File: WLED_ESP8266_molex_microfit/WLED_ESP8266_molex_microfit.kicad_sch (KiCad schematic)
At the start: 30 parts, among them J1 Molex Micro-fit 2x1, U1 ESP-12F, U2 AP6503, U3 TXS0102DCT, U4 TXS0102DCT

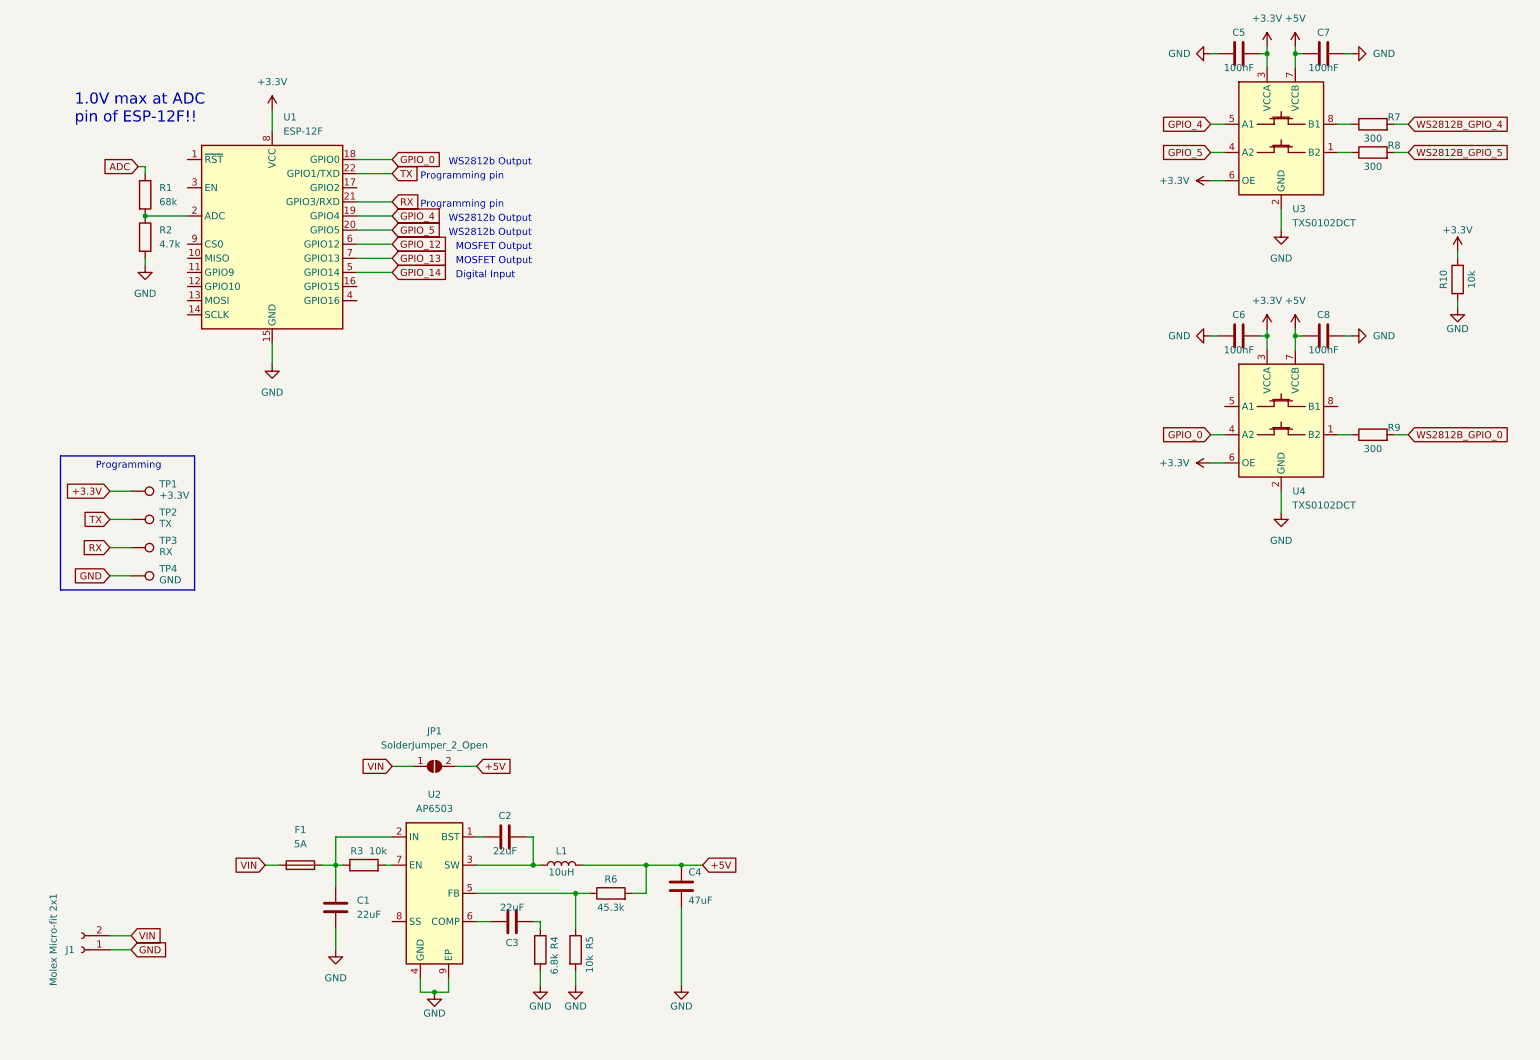
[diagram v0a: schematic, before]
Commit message: schematics updated
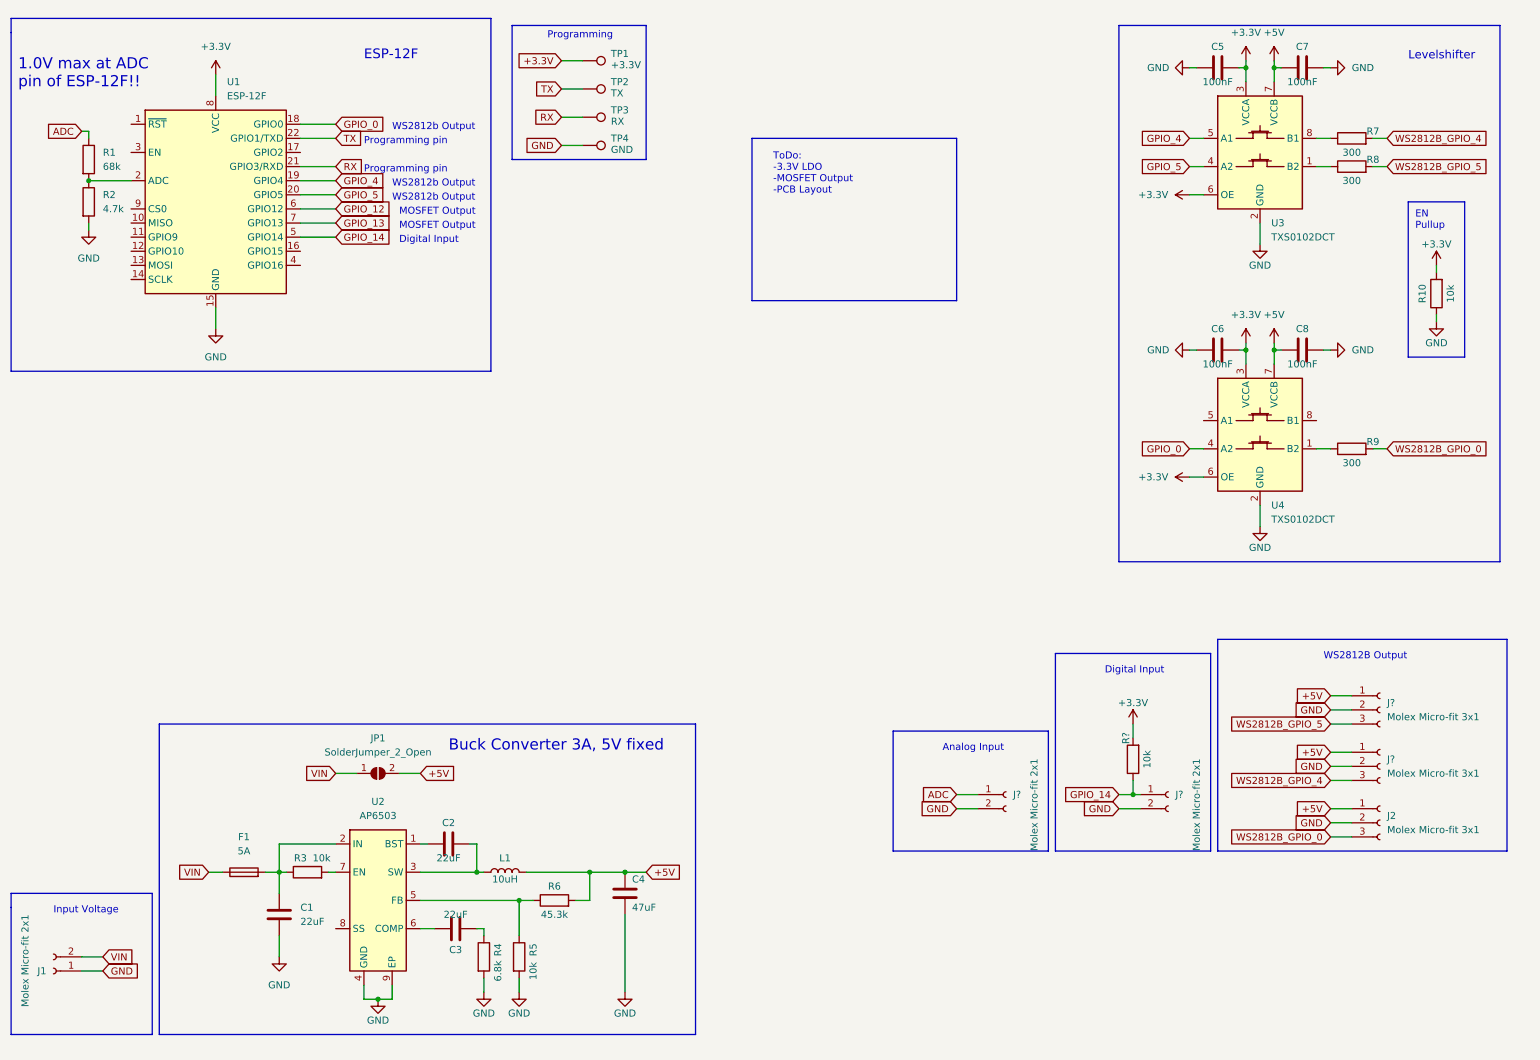
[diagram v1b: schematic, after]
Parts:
- added J2, J? (x2): Molex Micro-fit 3x1, Connector_Molex:Molex_Micro-Fit_3.0_43650-0300_1x03_P3.00mm_Horizontal, symbol Connector:Conn_01x03_Female
- added J? (x2): Molex Micro-fit 2x1, Connector_Molex:Molex_Micro-Fit_3.0_43650-0200_1x02_P3.00mm_Horizontal, symbol Connector:Conn_01x02_Female
- added R?: 10k, Capacitor_SMD:C_0603_1608Metric_Pad1.08x0.95mm_HandSolder, symbol Device:R
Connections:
- net +3V3: now also R?.2
- net +5V: now also J2.1 (Pin_1), J?.1 (Pin_1), J?.1 (Pin_1)
- net ADC: now also J?.1 (Pin_1)
- net GND: now also J2.2 (Pin_2), J?.2 (Pin_2), J?.2 (Pin_2), J?.2 (Pin_2), J?.2 (Pin_2)
- net GPIO_14: now also J?.1 (Pin_1), R?.1
- net WS2812B_GPIO_0: now also J2.3 (Pin_3)
- net WS2812B_GPIO_4: now also J?.3 (Pin_3)
- net WS2812B_GPIO_5: now also J?.3 (Pin_3)
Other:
- note added: "Analog Input"
- note added: "Buck Converter 3A, 5V fixed"
- note added: "EN Pullup"
- note added: "ESP-12F"
- note added: "Input Voltage"
- note added: "Levelshifter"
- note added: "ToDo: -3.3V LDO -MOSFET Output -PCB Layout"
- note added: "WS2812B Output"
- title: (none) -> WLED ESP8266 molex microfit
- moved on the sheet: C1, C2, C3, C4, C5, C6, C7, C8, F1, J1, JP1, L1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
